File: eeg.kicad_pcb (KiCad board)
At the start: 2 copper layers, 136 parts, among them J1 USB_B_Mini, U1 STM32F446RE, U10 -.+2.5V.+3.3V-GND, U11 +5V, U12 RN4678-V_RM100, U2 ADS1299-8CHANNEL, U3 LD39050PU33R, U4 TPS60403DBVT, U5 TPS73225DBVT, U6 TPS72325DBVT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

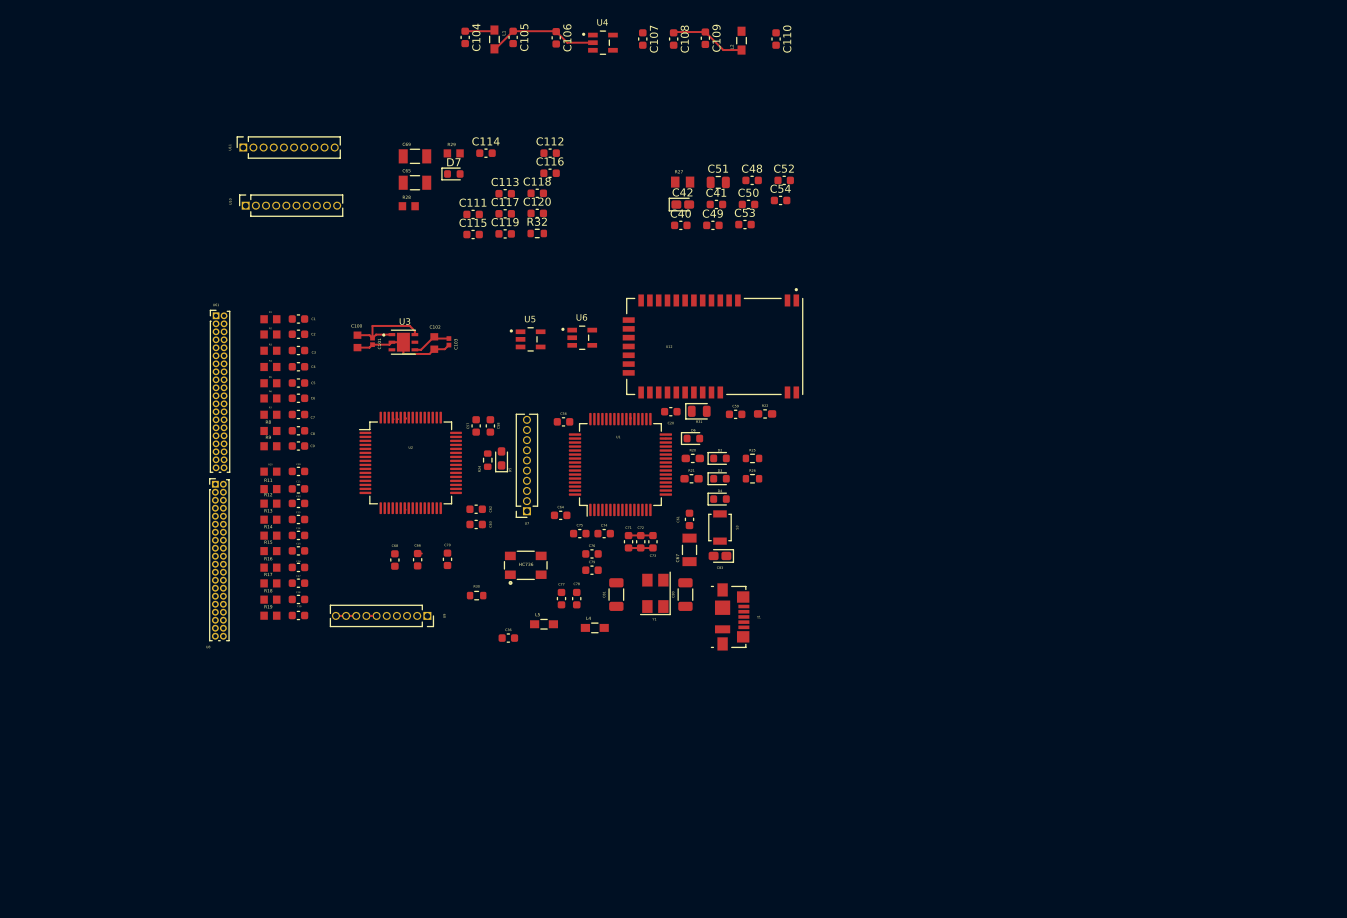
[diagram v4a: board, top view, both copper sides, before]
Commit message: ADS1299 Symbol and Footprint Changed, AVDD and ADSS PINS NEED TO FIX
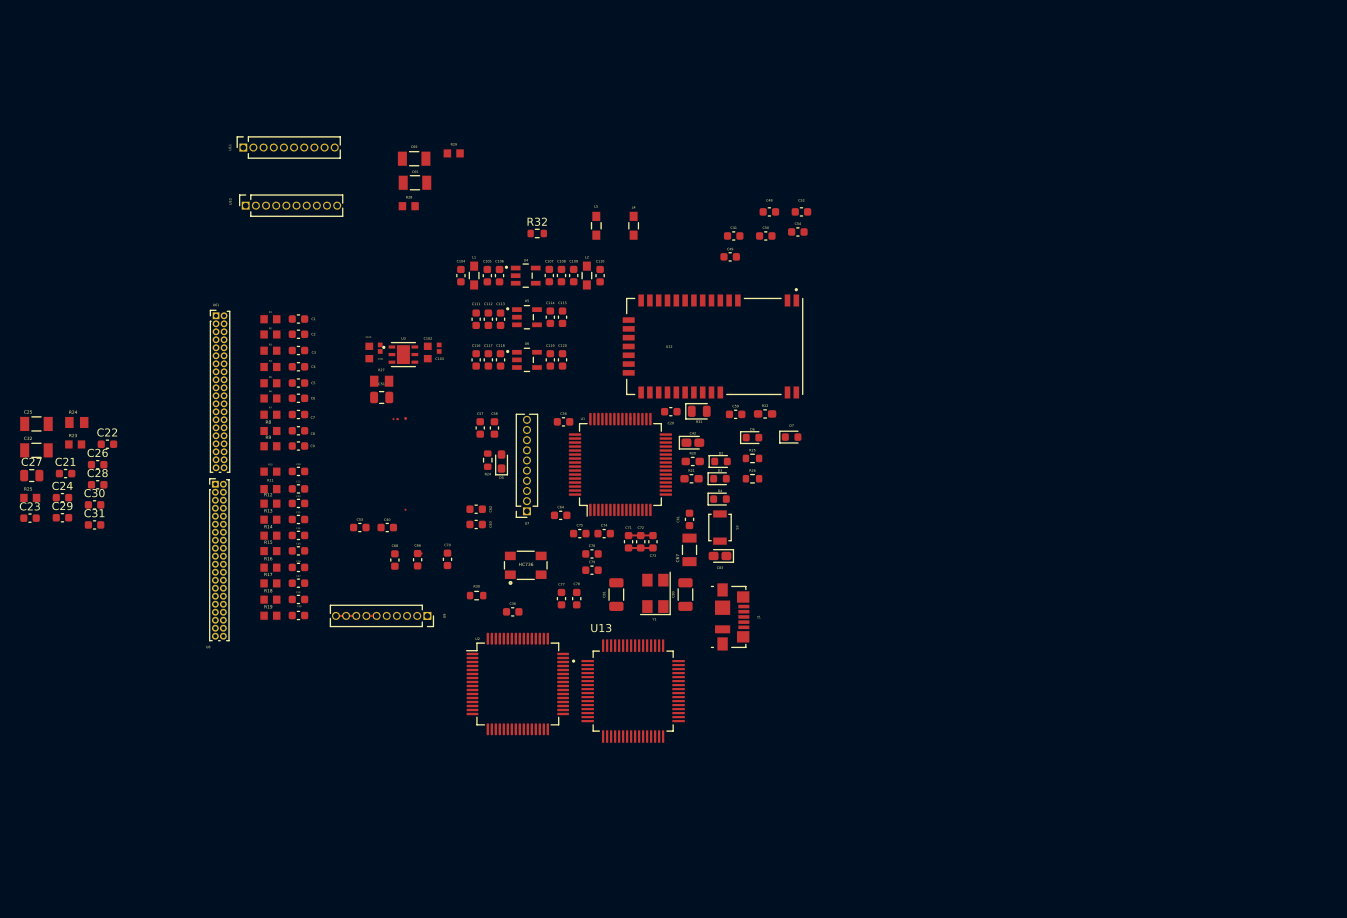
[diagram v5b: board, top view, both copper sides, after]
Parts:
- added C21: 100uF, Capacitor_SMD:C_0603_1608Metric, F.Cu at (21.1, 72.3)
- added C22: 1uF, Capacitor_SMD:C_0603_1608Metric, F.Cu at (26.3, 68.6)
- added C23: 0.1uF, Capacitor_SMD:C_0603_1608Metric, F.Cu at (16.6, 77.8)
- added C24: 1uF, Capacitor_SMD:C_0603_1608Metric, F.Cu at (20.7, 75.3)
- added C25: 10uF, TCA1C106M8R:RESC3216X65N, F.Cu at (17.4, 66.0)
- added C26: 1uF, Capacitor_SMD:C_0603_1608Metric, F.Cu at (25.1, 71.1)
- added C27: 1.5nF, Capacitor_SMD:C_0805_2012Metric, F.Cu at (16.8, 72.5)
- added C28: 0.1uF, Capacitor_SMD:C_0603_1608Metric, F.Cu at (25.1, 73.7)
- added C29: 0.1uF, Capacitor_SMD:C_0603_1608Metric, F.Cu at (20.7, 77.8)
- added C30: 1uF, Capacitor_SMD:C_0603_1608Metric, F.Cu at (24.7, 76.2)
- added C31: 1uF, Capacitor_SMD:C_0603_1608Metric, F.Cu at (24.7, 78.7)
- added C32: 100uF, TCA1C106M8R:RESC3216X65N, F.Cu at (17.4, 69.3)
- added R23: 10K, ERA-3A:RESC1608X55N, F.Cu at (22.3, 68.6)
- added R24: 1M, ERA-6AEB105V:RESC2012X60N, F.Cu at (22.5, 65.9)
- added R25: 10K, ERA-3A:RESC1608X55N, F.Cu at (16.6, 75.3)
- added U13: ADS1299IPAG, QFP50P1200X1200X120-64N, F.Cu at (92.0, 99.4)
- moved C53 61.3 mm to (57.8, 79.0)
- moved D7 53.5 mm to (111.8, 67.7)
- moved C40 52.7 mm to (61.3, 79.0)
- moved L4 50.5 mm to (92.1, 41.3), turned to 270 degrees
- moved L5 50.2 mm to (87.4, 41.3), turned to 270 degrees
- moved C51 49.9 mm to (60.6, 62.7)
- moved R27 45.1 mm to (60.6, 60.7)
- moved C110 36.9 mm to (87.9, 47.5)
- moved L2 35.2 mm to (86.2, 47.5)
- moved C109 33.9 mm to (84.6, 47.5)
- moved C108 32.7 mm to (83.1, 47.5)
- moved C107 31.8 mm to (81.5, 47.5)
- moved U2 30.7 mm to (77.6, 98.6)
- moved U4 30.7 mm to (78.6, 47.5)
- moved C106 30.6 mm to (75.3, 47.5)
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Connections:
- C105 pad 2: Net-(C105-Pad2) -> GND
- C106 pad 2: Net-(C105-Pad2) -> GND
- U2 pad 18: /SRB2 -> Net-(U2-Pad18)
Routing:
- net +5V: track 15.9 -> 0.00 mm
- net Net-(C105-Pad1): track 13.8 -> 0.00 mm
- net Net-(C100-Pad2): track 13.6 -> 0.00 mm
- net Net-(C108-Pad1): track 9.46 -> 0.00 mm
- net +3V3: track 8.24 -> 3.23 mm

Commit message: Footprints edited and aligned
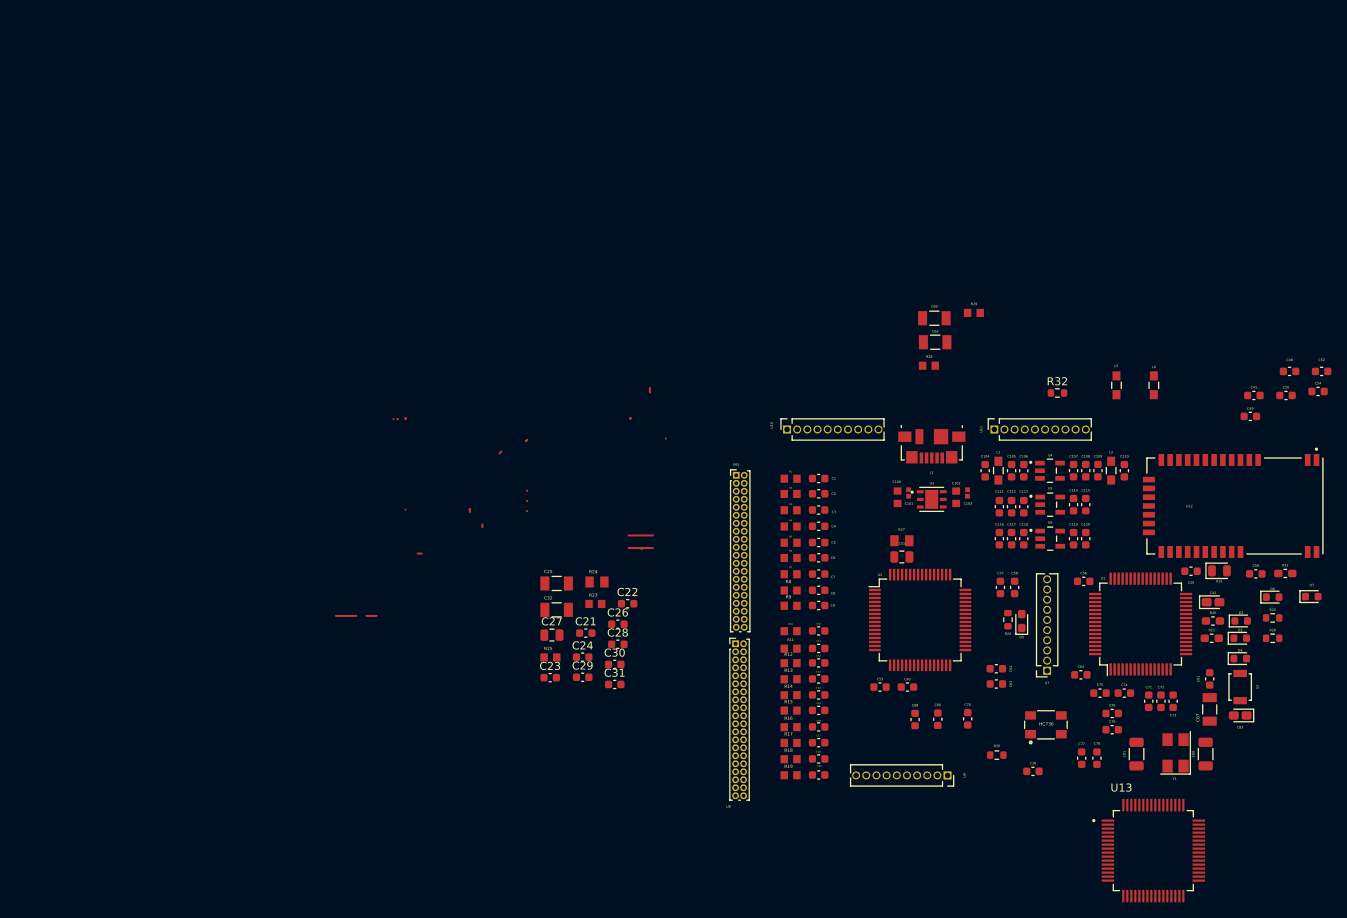
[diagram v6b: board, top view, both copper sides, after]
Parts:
- moved U11 100.3 mm to (137.2, 66.7)
- moved U10 73.2 mm to (111.3, 66.7)
- moved C104 69.9 mm to (136.0, 71.9)
- moved C107 69.9 mm to (147.1, 71.9)
- moved C108 69.9 mm to (148.6, 71.9)
- moved C109 69.9 mm to (150.1, 71.9)
- moved C110 69.9 mm to (153.4, 71.9)
- moved L1 69.9 mm to (137.7, 71.9)
- moved U4 69.9 mm to (144.1, 71.9)
- moved C105 69.9 mm to (139.3, 71.9)
- moved C106 69.9 mm to (140.8, 71.9)
- moved L2 69.9 mm to (151.8, 71.9)
- moved U5 69.5 mm to (144.1, 76.1)
- moved C114 69.5 mm to (147.1, 76.1)
- moved C115 69.5 mm to (148.6, 76.1)
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
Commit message: Electrodes footprint 2.54mm to 1.27mm
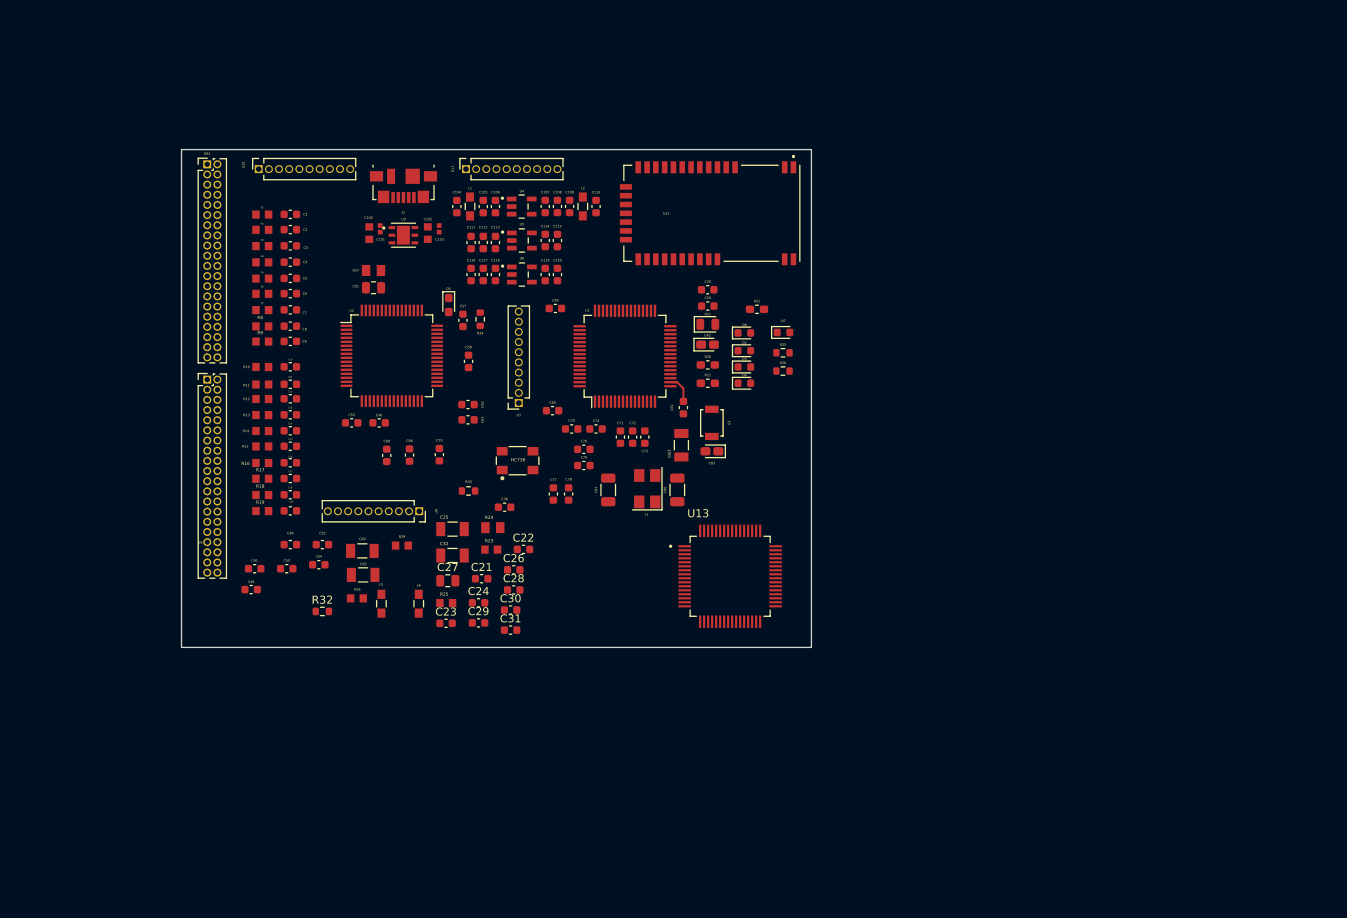
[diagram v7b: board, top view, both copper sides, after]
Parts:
- U61, U8: footprint Connector_PinHeader_1.00mm:PinHeader_2x20_P1.00mm_Vertical -> Connector_PinHeader_1.27mm:PinHeader_2x20_P1.27mm_Vertical
- moved C41 126.8 mm to (44.7, 84.1)
- moved C48 126.8 mm to (49.2, 81.1)
- moved C49 126.8 mm to (44.3, 86.8)
- moved C54 126.8 mm to (52.7, 83.6)
- moved C52 126.8 mm to (53.2, 81.1)
- moved C50 126.8 mm to (48.7, 84.1)
- moved R32 95.9 mm to (53.2, 89.5)
- moved L4 95.9 mm to (65.2, 88.5)
- moved L5 95.9 mm to (60.5, 88.5)
- moved D5 81.8 mm to (69.0, 51.2), turned to 270 degrees
- moved C65 77.2 mm to (58.3, 84.9)
- moved C69 77.2 mm to (58.2, 81.9)
- moved R28 77.2 mm to (57.5, 87.9)
- moved R29 77.2 mm to (63.1, 81.3)
- moved U61 76.7 mm to (38.8, 33.6)
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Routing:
- net +3V3: track 3.23 -> 0.38 mm
- net /VREFP: track 2.54 -> 0.00 mm
- net -2V5: track 1.42 -> 0.00 mm
- net /USART6_RX: track 0.76 -> 0.00 mm
- net GNDREF: track 4.32 -> 3.57 mm
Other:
- board outline added: 78.7 x 62.2 mm

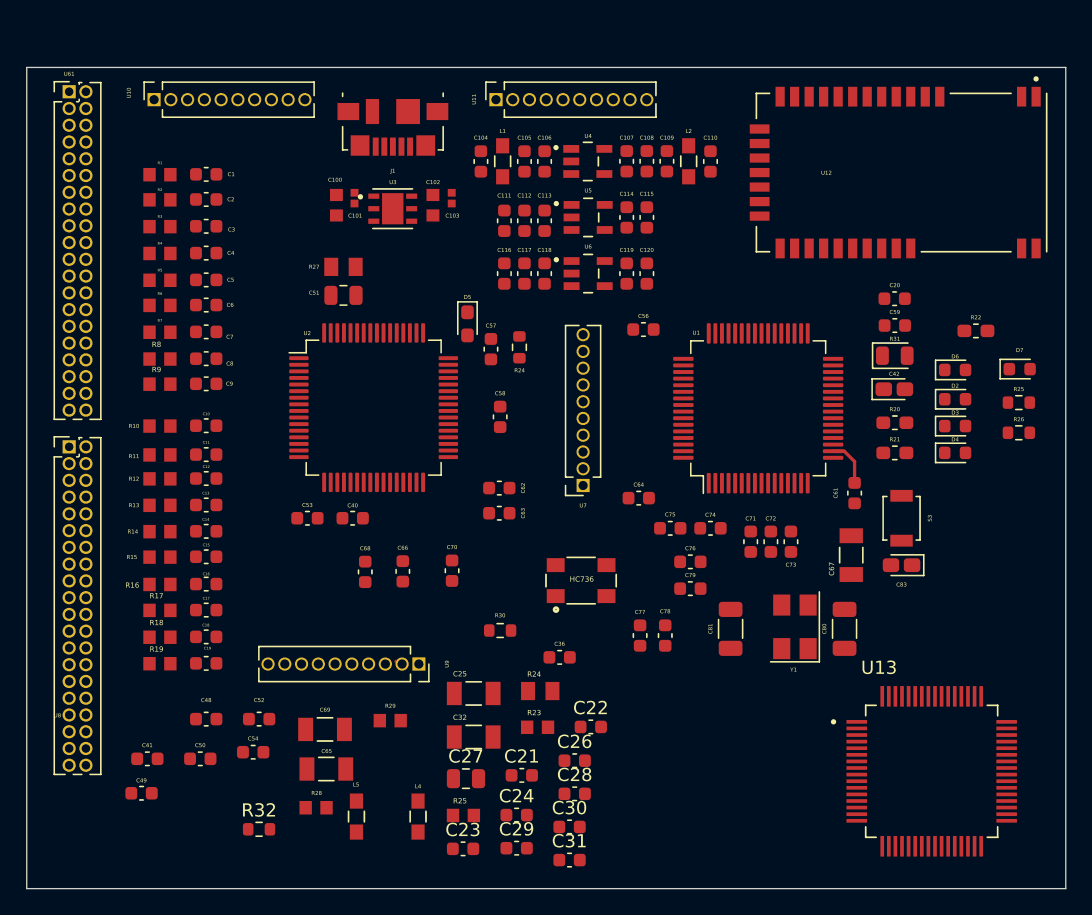
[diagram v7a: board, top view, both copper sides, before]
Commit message: Electrode1 and electrode2 schematics are fixed
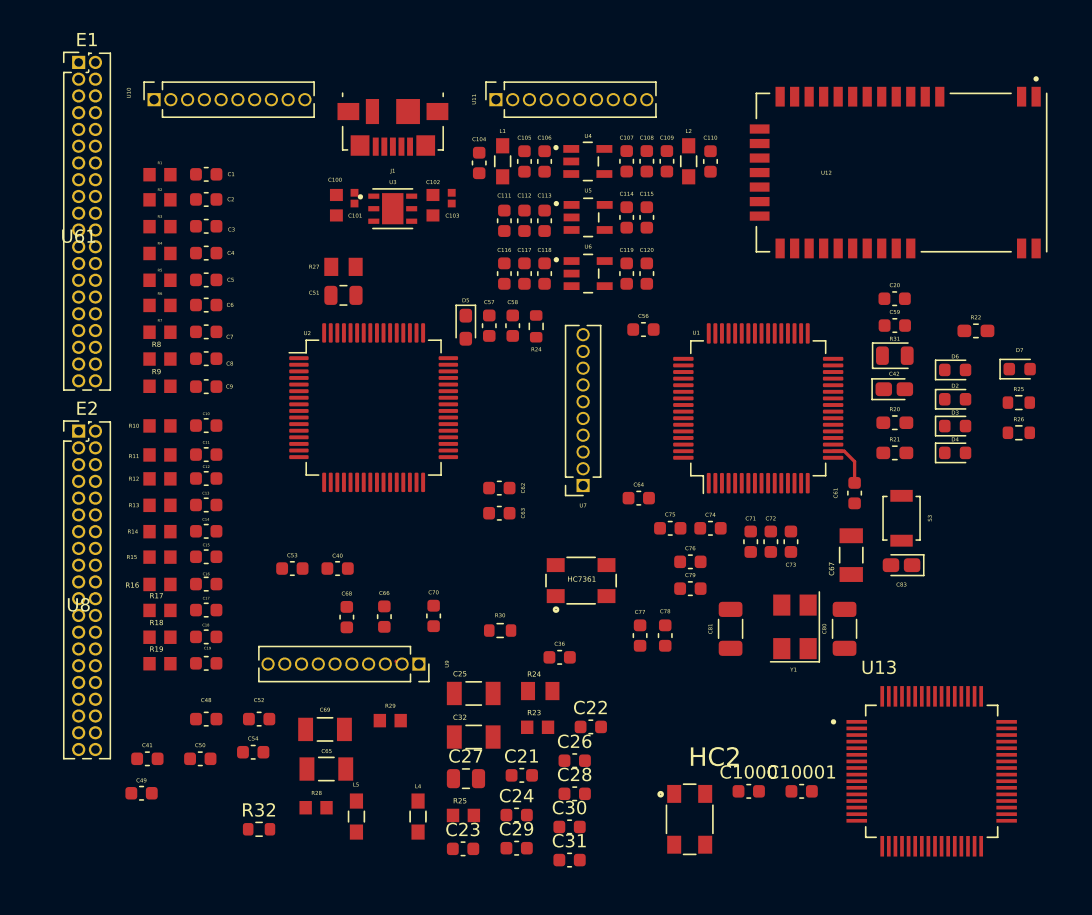
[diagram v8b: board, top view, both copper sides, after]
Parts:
- added C1000: 0.1uF, Capacitor_SMD:C_0603_1608Metric, F.Cu at (90.3, 86.6)
- added C10001: 1uF, Capacitor_SMD:C_0603_1608Metric, F.Cu at (94.3, 86.6)
- added HC2: 2.048mhz, ERA-3A:OSCCC500X320X150N, F.Cu at (85.8, 88.7)
- U61: value Electrode2 -> Electrode1; footprint Connector_PinHeader_1.27mm:PinHeader_2x20_P1.27mm_Vertical -> ADS1299IPAG:openldhardware
- U8: value Electrode1 -> Electrode2; footprint Connector_PinHeader_1.27mm:PinHeader_2x20_P1.27mm_Vertical -> ADS1299IPAG:openldhardware
- moved U8 11.5 mm to (39.5, 72.0)
- moved U61 10.5 mm to (39.5, 44.1)
- moved C58 6.97 mm to (72.4, 51.3)
- moved C40 3.98 mm to (59.1, 69.7)
- moved C53 3.98 mm to (55.7, 69.7)
- moved C66 3.70 mm to (62.7, 73.4)
- moved C68 3.70 mm to (59.8, 73.4)
- moved C70 3.70 mm to (66.4, 73.3)
- moved R24 2.03 mm to (74.2, 51.4)
- moved C57 1.78 mm to (70.6, 51.3)
- moved D5 0.28 mm to (68.8, 51.4)
- moved C9 0.21 mm to (49.2, 55.9)
- moved C104 0.17 mm to (69.8, 39.0)
- moved R9 0.16 mm to (45.7, 55.9)
- renumbered HC736 to HC7361
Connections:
- C100 pad 2: Net-(C100-Pad2) -> GND
- C101 pad 2: Net-(C100-Pad2) -> GND
- C102 pad 2: Net-(C100-Pad2) -> GND
- C103 pad 2: Net-(C100-Pad2) -> GND
- U12 pad 15: /RN46_CTS -> /RN46CTS
- U13 pad 39: Net-(U13-Pad39) -> CS
- U13 pad 52: Net-(U13-Pad52) -> GND
- U3 pad 2: Net-(C100-Pad2) -> GND
- U3 pad 7: Net-(C100-Pad2) -> GND
- U61 pad 10: /CIN8N -> /-2.5V
- U61 pad 11: /-2.5V -> /+2.5V
- U61 pad 12: GND -> /-2.5V
- U61 pad 14: /CIN8P -> /-2.5V
- U61 pad 15: /-2.5V -> /+2.5V
- U61 pad 16: GND -> /-2.5V
- U61 pad 18: /CIN7N -> /-2.5V
- U61 pad 19: /-2.5V -> /+2.5V
- U61 pad 2: /BIASINV -> /-2.5V
- U61 pad 20: GND -> /-2.5V
- U61 pad 21: /+2.5V -> /CSRB2
- U61 pad 22: /CIN7P -> GND
- U61 pad 23: /-2.5V -> /CSRB1
- U61 pad 25: /+2.5V -> /CIN1P
- U61 pad 26: /CIN6N -> GND
- U61 pad 27: /-2.5V -> /CIN1N
- U61 pad 29: /+2.5V -> /CIN2P
- U61 pad 3: /-2.5V -> /+2.5V
- U61 pad 30: /CIN6P -> GND
- U61 pad 31: /-2.5V -> /CIN2N
- U61 pad 33: /+2.5V -> /CIN3P
- U61 pad 34: /CIN5N -> GND
- U61 pad 35: /-2.5V -> /CIN3N
- U61 pad 37: /+2.5V -> /CIN4P
- U61 pad 38: /CIN5P -> GND
- U61 pad 39: /-2.5V -> /CIN4N
- U61 pad 4: GND -> /-2.5V
- U61 pad 6: /CBIAS -> /-2.5V
- U61 pad 7: /-2.5V -> /+2.5V
- U61 pad 8: GND -> /-2.5V
- U8 pad 10: /CIN3N -> /-2.5V
- U8 pad 11: /-2.5V -> /+2.5V
- U8 pad 12: GND -> /-2.5V
- U8 pad 14: /CIN3P -> /-2.5V
- U8 pad 15: /-2.5V -> /+2.5V
- U8 pad 16: GND -> /-2.5V
- U8 pad 18: /CIN2N -> /-2.5V
- U8 pad 19: /-2.5V -> /+2.5V
- U8 pad 2: /CIN4N -> /-2.5V
- U8 pad 20: GND -> /-2.5V
- U8 pad 21: /+2.5V -> GND
- U8 pad 22: /CIN2P -> /CIN5P
- U8 pad 23: /-2.5V -> GND
- U8 pad 24: GND -> /CIN5N
- U8 pad 25: /+2.5V -> GND
- U8 pad 26: /CIN1N -> /CIN6P
- U8 pad 27: /-2.5V -> GND
- U8 pad 28: GND -> /CIN6N
- U8 pad 29: /+2.5V -> GND
- U8 pad 3: /-2.5V -> /+2.5V
- U8 pad 30: /CIN1P -> /CIN7P
- U8 pad 31: /-2.5V -> GND
- U8 pad 32: GND -> /CIN7N
- U8 pad 33: /+2.5V -> GND
- U8 pad 34: /CSRB1 -> /CIN8P
- U8 pad 35: /-2.5V -> GND
- U8 pad 36: GND -> /CIN8N
- U8 pad 37: /+2.5V -> GND
- U8 pad 38: /CSRB2 -> /CBIAS
- U8 pad 39: /-2.5V -> GND
- U8 pad 4: GND -> /-2.5V
- U8 pad 40: GND -> /BIASINV
- U8 pad 6: /CIN4P -> /-2.5V
- U8 pad 7: /-2.5V -> /+2.5V
- U8 pad 8: GND -> /-2.5V
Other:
- board outline removed
